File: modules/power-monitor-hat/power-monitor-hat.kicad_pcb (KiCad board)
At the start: 2 copper layers, 65 x 56 mm, 56 parts, among them J1 Barrel_Jack_Switch, J2 GPIO, J3 OutputTerminal, J4 OutputTerminal, J5 OutputTerminal, Q1 BC856BDW1, Q2 SI2301CDS, U1 NCP1117-3.3_SOT223, U2 CAT24C256, U3 INA219AxD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

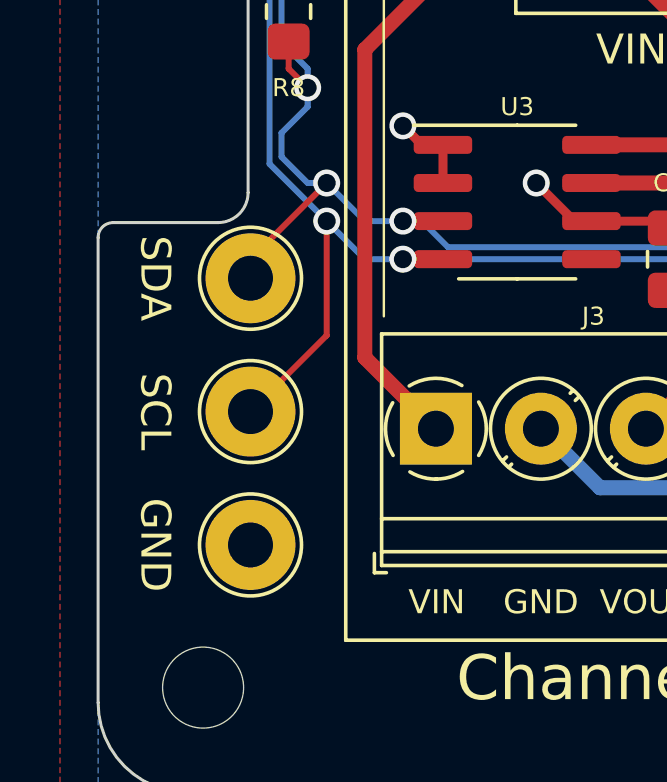
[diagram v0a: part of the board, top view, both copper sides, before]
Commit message: Use smaller footprint for test points
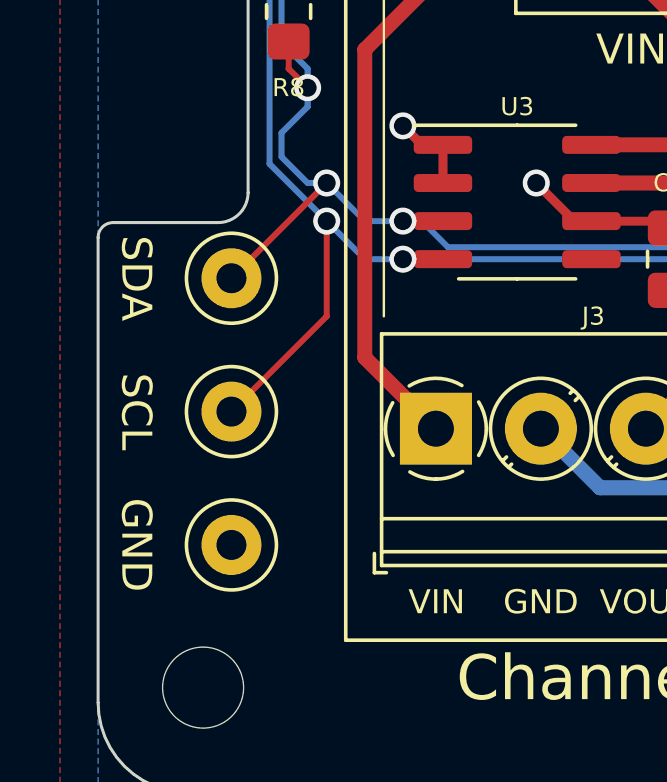
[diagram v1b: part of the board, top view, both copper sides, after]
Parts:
- TP1, TP2, TP3: footprint TestPoint:TestPoint_Loop_D2.54mm_Drill1.5mm_Beaded -> TestPoint:TestPoint_Loop_D1.80mm_Drill1.0mm_Beaded
- moved TP1 0.64 mm to (104.4, 91.7)
- moved TP2 0.64 mm to (104.4, 82.9)
- moved TP3 0.64 mm to (104.4, 87.3)
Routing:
- net /SDA: track 96.1 -> 97.0 mm
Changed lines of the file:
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@@
     )
   )
-  (footprint "TestPoint:TestPoint_Loop_D2.54mm_Drill1.5mm_Beaded" (layer "F.Cu")
-    (at 105.08 91.745)
-    (descr "wire loop with bead as test point, loop diameter2.548mm, hole diameter 1.5mm")
+  (footprint "TestPoint:TestPoint_Loop_D1.80mm_Drill1.0mm_Beaded" (layer "F.Cu")
+    (at 104.445 91.745)
+    (descr "wire loop with bead as test point, loop diameter 1.8mm, hole diameter 1.0mm")
     (tags "test point wire loop bead")
     (property "Sheetfile" "power-monitor-hat.kicad_sch")
@@
       (effects (font (size 0.6 0.6) (thickness 0.08)))
     )
-    (fp_circle (center 0 0) (end 1.7 0) (layer "F.SilkS") (width 0.12) (fill none))
-    (fp_circle (center 0 0) (end 2 0) (layer "F.CrtYd") (width 0.05) (fill none))
-    (fp_line (start -1.3 -0.3) (end -1.3 0.3) (layer "F.Fab") (width 0.12))
-    (fp_line (start 1.3 0.3) (end 1.3 -0.3) (layer "F.Fab") (width 0.12))
-    (fp_line (start -1.3 0.3) (end 1.3 0.3) (layer "F.Fab") (width 0.12))
-    (fp_line (start 1.3 -0.3) (end -1.3 -0.3) (layer "F.Fab") (width 0.12))
-    (fp_circle (center 0 0) (end 1.5 0) (layer "F.Fab") (width 0.12) (fill none))
-    (pad "1" thru_hole circle (at 0 0) (size 3 3) (drill 1.5) (layers *.Cu *.Mask)
+    (fp_circle (center 0 0) (end 1.5 0) (layer "F.SilkS") (width 0.12) (fill none))
+    (fp_circle (center 0 0) (end 1.8 0) (layer "F.CrtYd") (width 0.05) (fill none))
+    (fp_line (start 0.9 -0.2) (end 0.9 0.2) (layer "F.Fab") (width 0.12))
+    (fp_line (start 0.9 0.2) (end -0.9 0.2) (layer "F.Fab") (width 0.12))
+    (fp_line (start -0.9 -0.2) (end 0.9 -0.2) (layer "F.Fab") (width 0.12))
+    (fp_line (start -0.9 0.2) (end -0.9 -0.2) (layer "F.Fab") (width 0.12))
+    (fp_circle (center 0 0) (end 1.3 0) (layer "F.Fab") (width 0.12) (fill none))
+    (pad "1" thru_hole circle (at 0 0) (size 2 2) (drill 1) (layers *.Cu *.Mask)
       (net 1 "GND") (pinfunction "1") (pintype "passive"))
-    (model "${KICAD6_3DMODEL_DIR}/TestPoint.3dshapes/TestPoint_Loop_D2.54mm_Drill1.5mm_Beaded.wrl"
+    (model "${KICAD6_3DMODEL_DIR}/TestPoint.3dshapes/TestPoint_Loop_D1.80mm_Drill1.0mm_Beaded.wrl"
       (offset (xyz 0 0 0))
       (scale (xyz 1 1 1))
@@
     )
   )
-  (footprint "TestPoint:TestPoint_Loop_D2.54mm_Drill1.5mm_Beaded" (layer "F.Cu")
-    (at 105.08 87.3)
-    (descr "wire loop with bead as test point, loop diameter2.548mm, hole diameter 1.5mm")
+  (footprint "TestPoint:TestPoint_Loop_D1.80mm_Drill1.0mm_Beaded" (layer "F.Cu")
+    (at 104.445 87.3)
+    (descr "wire loop with bead as test point, loop diameter 1.8mm, hole diameter 1.0mm")
     (tags "test point wire loop bead")
     (property "Sheetfile" "power-monitor-hat.kicad_sch")
@@
       (effects (font (size 0.6 0.6) (thickness 0.08)))
     )
-    (fp_circle (center 0 0) (end 1.7 0) (layer "F.SilkS") (width 0.12) (fill none))
-    (fp_circle (center 0 0) (end 2 0) (layer "F.CrtYd") (width 0.05) (fill none))
-    (fp_line (start -1.3 -0.3) (end -1.3 0.3) (layer "F.Fab") (width 0.12))
-    (fp_line (start 1.3 -0.3) (end -1.3 -0.3) (layer "F.Fab") (width 0.12))
-    (fp_line (start -1.3 0.3) (end 1.3 0.3) (layer "F.Fab") (width 0.12))
-    (fp_line (start 1.3 0.3) (end 1.3 -0.3) (layer "F.Fab") (width 0.12))
-    (fp_circle (center 0 0) (end 1.5 0) (layer "F.Fab") (width 0.12) (fill none))
-    (pad "1" thru_hole circle (at 0 0) (size 3 3) (drill 1.5) (layers *.Cu *.Mask)
+    (fp_circle (center 0 0) (end 1.5 0) (layer "F.SilkS") (width 0.12) (fill none))
+    (fp_circle (center 0 0) (end 1.8 0) (layer "F.CrtYd") (width 0.05) (fill none))
+    (fp_line (start -0.9 -0.2) (end 0.9 -0.2) (layer "F.Fab") (width 0.12))
+    (fp_line (start -0.9 0.2) (end -0.9 -0.2) (layer "F.Fab") (width 0.12))
+    (fp_line (start 0.9 -0.2) (end 0.9 0.2) (layer "F.Fab") (width 0.12))
+    (fp_line (start 0.9 0.2) (end -0.9 0.2) (layer "F.Fab") (width 0.12))
+    (fp_circle (center 0 0) (end 1.3 0) (layer "F.Fab") (width 0.12) (fill none))
+    (pad "1" thru_hole circle (at 0 0) (size 2 2) (drill 1) (layers *.Cu *.Mask)
       (net 2 "/SCL") (pinfunction "1") (pintype "passive"))
-    (model "${KICAD6_3DMODEL_DIR}/TestPoint.3dshapes/TestPoint_Loop_D2.54mm_Drill1.5mm_Beaded.wrl"
+    (model "${KICAD6_3DMODEL_DIR}/TestPoint.3dshapes/TestPoint_Loop_D1.80mm_Drill1.0mm_Beaded.wrl"
       (offset (xyz 0 0 0))
       (scale (xyz 1 1 1))
@@
     )
   )
-  (footprint "TestPoint:TestPoint_Loop_D2.54mm_Drill1.5mm_Beaded" (layer "F.Cu")
-    (at 105.08 82.855)
-    (descr "wire loop with bead as test point, loop diameter2.548mm, hole diameter 1.5mm")
+  (footprint "TestPoint:TestPoint_Loop_D1.80mm_Drill1.0mm_Beaded" (layer "F.Cu")
+    (at 104.445 82.855)
+    (descr "wire loop with bead as test point, loop diameter 1.8mm, hole diameter 1.0mm")
     (tags "test point wire loop bead")
     (property "Sheetfile" "power-monitor-hat.kicad_sch")
@@
       (effects (font (size 0.6 0.6) (thickness 0.08)))
     )
-    (fp_circle (center 0 0) (end 1.7 0) (layer "F.SilkS") (width 0.12) (fill none))
-    (fp_circle (center 0 0) (end 2 0) (layer "F.CrtYd") (width 0.05) (fill none))
-    (fp_line (start 1.3 -0.3) (end -1.3 -0.3) (layer "F.Fab") (width 0.12))
-    (fp_line (start 1.3 0.3) (end 1.3 -0.3) (layer "F.Fab") (width 0.12))
-    (fp_line (start -1.3 -0.3) (end -1.3 0.3) (layer "F.Fab") (width 0.12))
-    (fp_line (start -1.3 0.3) (end 1.3 0.3) (layer "F.Fab") (width 0.12))
-    (fp_circle (center 0 0) (end 1.5 0) (layer "F.Fab") (width 0.12) (fill none))
-    (pad "1" thru_hole circle (at 0 0) (size 3 3) (drill 1.5) (layers *.Cu *.Mask)
+    (fp_circle (center 0 0) (end 1.5 0) (layer "F.SilkS") (width 0.12) (fill none))
+    (fp_circle (center 0 0) (end 1.8 0) (layer "F.CrtYd") (width 0.05) (fill none))
+    (fp_line (start -0.9 0.2) (end -0.9 -0.2) (layer "F.Fab") (width 0.12))
+    (fp_line (start 0.9 0.2) (end -0.9 0.2) (layer "F.Fab") (width 0.12))
+    (fp_line (start -0.9 -0.2) (end 0.9 -0.2) (layer "F.Fab") (width 0.12))
+    (fp_line (start 0.9 -0.2) (end 0.9 0.2) (layer "F.Fab") (width 0.12))
+    (fp_circle (center 0 0) (end 1.3 0) (layer "F.Fab") (width 0.12) (fill none))
+    (pad "1" thru_hole circle (at 0 0) (size 2 2) (drill 1) (layers *.Cu *.Mask)
       (net 43 "/SDA") (pinfunction "1") (pintype "passive"))
-    (model "${KICAD6_3DMODEL_DIR}/TestPoint.3dshapes/TestPoint_Loop_D2.54mm_Drill1.5mm_Beaded.wrl"
+    (model "${KICAD6_3DMODEL_DIR}/TestPoint.3dshapes/TestPoint_Loop_D1.80mm_Drill1.0mm_Beaded.wrl"
       (offset (xyz 0 0 0))
       (scale (xyz 1 1 1))
@@
   (via (at 129.21 77.775) (size 0.9) (drill 0.6) (layers "F.Cu" "B.Cu") (free) (net 1))
   (via (at 133.655 79.68) (size 0.9) (drill 0.6) (layers "F.Cu" "B.Cu") (free) (net 1))
-  (segment (start 107.62 80.95) (end 107.62 84.76) (width 0.2) (layer "F.Cu") (net 2))
   (segment (start 106.35 66.98) (end 105.715 66.345) (width 0.2) (layer "F.Cu") (net 2))
-  (segment (start 107.62 84.76) (end 105.08 87.3) (width 0.2) (layer "F.Cu") (net 2))
+  (segment (start 107.62 84.125) (end 104.445 87.3) (width 0.2) (layer "F.Cu") (net 2))
+  (segment (start 107.62 80.95) (end 107.62 84.125) (width 0.2) (layer "F.Cu") (net 2))
   (segment (start 130.545 82.22) (end 129.21 82.22) (width 0.2) (layer "F.Cu") (net 2))
   (segment (start 110.16 82.22) (end 111.495 82.22) (width 0.2) (layer "F.Cu") (net 2))
@@
   (segment (start 154.545 78.41) (end 159.69 78.41) (width 0.5) (layer "F.Cu") (net 38))
   (segment (start 158.42 65.71) (end 158.42 72.68) (width 0.5) (layer "F.Cu") (net 39))
-  (segment (start 107.62 79.68) (end 105.08 82.22) (width 0.2) (layer "F.Cu") (net 43))
   (segment (start 110.16 80.95) (end 111.495 80.95) (width 0.2) (layer "F.Cu") (net 43))
   (segment (start 106.35 74.965) (end 106.35 75.87) (width 0.2) (layer "F.Cu") (net 43))
@@
   (segment (start 149.595 79.68) (end 149.595 80.95) (width 0.2) (layer "F.Cu") (net 43))
   (segment (start 106.35 75.87) (end 106.985 76.505) (width 0.2) (layer "F.Cu") (net 43))
+  (segment (start 107.62 79.68) (end 104.445 82.855) (width 0.2) (layer "F.Cu") (net 43))
   (via (at 106.985 76.505) (size 0.9) (drill 0.6) (layers "F.Cu" "B.Cu") (net 43))
   (via (at 110.16 80.95) (size 0.9) (drill 0.6) (layers "F.Cu" "B.Cu") (net 43))

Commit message: Correct units
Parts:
- C2, C3: value 22u -> 10u
- R10, R12, R14, R3, R4: value 220R -> 470R
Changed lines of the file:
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@@
       (effects (font (size 0.6 0.6) (thickness 0.08)))
     )
-    (fp_text value "220R" (at 2.385 0) (layer "F.Fab")
+    (fp_text value "470R" (at 2.385 0) (layer "F.Fab")
       (effects (font (size 0.6 0.6) (thickness 0.08)))
     )
@@
       (effects (font (size 0.6 0.6) (thickness 0.08)))
     )
-    (fp_text value "22u" (at 0 -1.905) (layer "F.Fab")
+    (fp_text value "10u" (at 0 -1.905) (layer "F.Fab")
       (effects (font (size 0.6 0.6) (thickness 0.08)))
     )
@@
       (effects (font (size 0.6 0.6) (thickness 0.08)))
     )
-    (fp_text value "220R" (at 2.385 0) (layer "F.Fab")
+    (fp_text value "470R" (at 2.385 0) (layer "F.Fab")
       (effects (font (size 0.6 0.6) (thickness 0.08)))
     )
@@
       (effects (font (size 0.6 0.6) (thickness 0.08)))
     )
-    (fp_text value "220R" (at 3.175 0) (layer "F.Fab")
+    (fp_text value "470R" (at 3.175 0) (layer "F.Fab")
       (effects (font (size 0.6 0.6) (thickness 0.08)))
     )
@@
       (effects (font (size 0.6 0.6) (thickness 0.08)))
     )
-    (fp_text value "220R" (at 3.175 0) (layer "F.Fab")
+    (fp_text value "470R" (at 3.175 0) (layer "F.Fab")
       (effects (font (size 0.6 0.6) (thickness 0.08)))
     )
@@
       (effects (font (size 0.6 0.6) (thickness 0.08)))
     )
-    (fp_text value "220R" (at 3.175 0) (layer "F.Fab")
+    (fp_text value "470R" (at 3.175 0) (layer "F.Fab")
       (effects (font (size 0.6 0.6) (thickness 0.08)))
     )
@@
       (effects (font (size 0.6 0.6) (thickness 0.08)))
     )
-    (fp_text value "22u" (at 0 1.905) (layer "F.Fab")
-      (effects (font (size 0.6 0.6) (thickness 0.08)))
-    )
+    (fp_text value "10u" (at 0 1.905) (layer "F.Fab")
+      (effects (font (size 0.6 0.6) (thickness 0.08)))
+    )

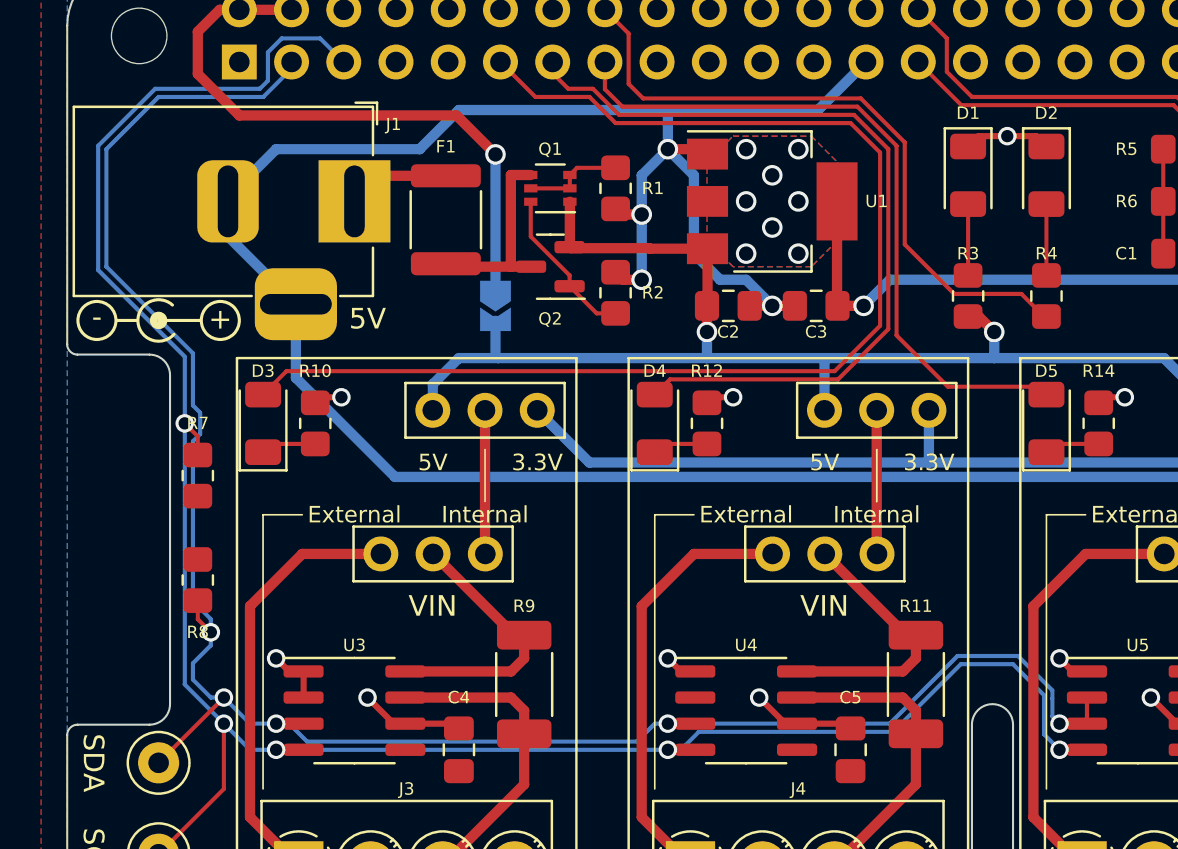
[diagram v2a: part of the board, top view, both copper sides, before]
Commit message: Prevent silk over via
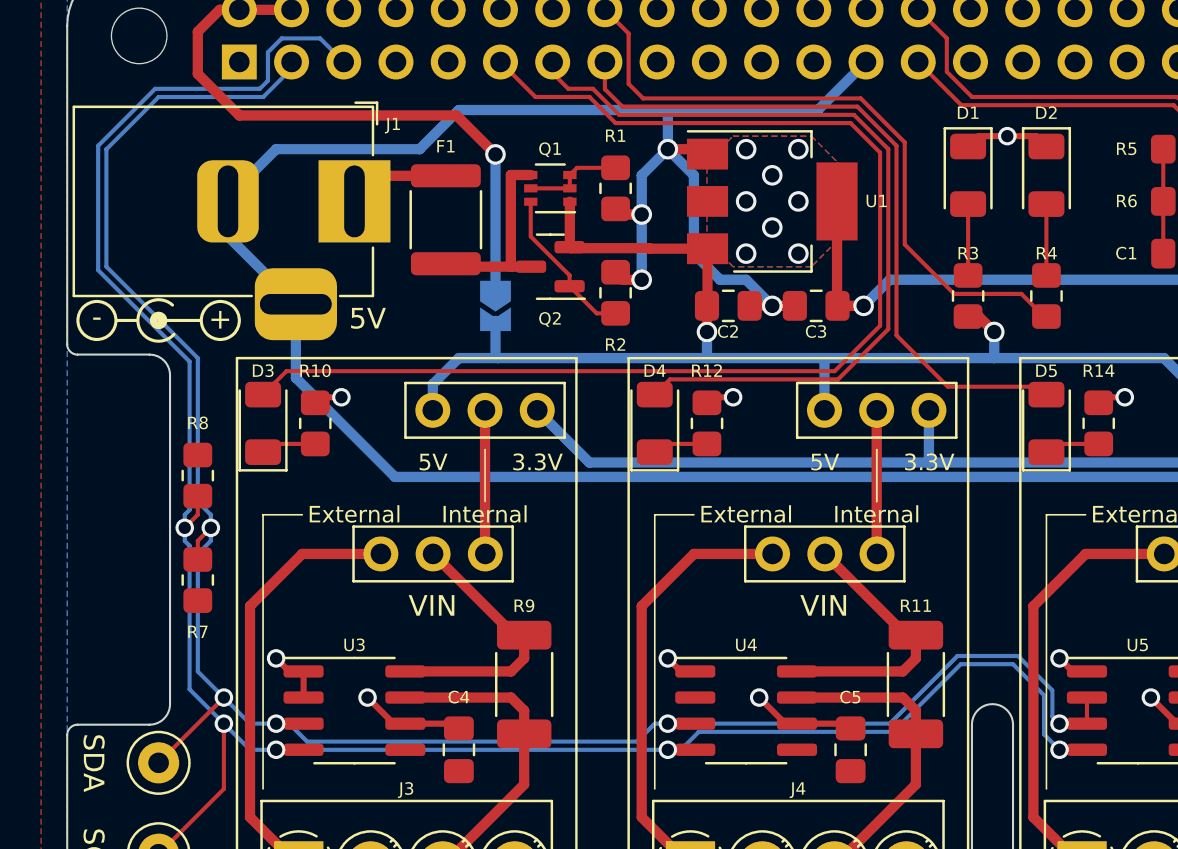
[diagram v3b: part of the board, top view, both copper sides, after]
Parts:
- turned R7 to 90 degrees
- turned R8 to -90 degrees
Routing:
- net /SDA: track 97.0 -> 96.1 mm

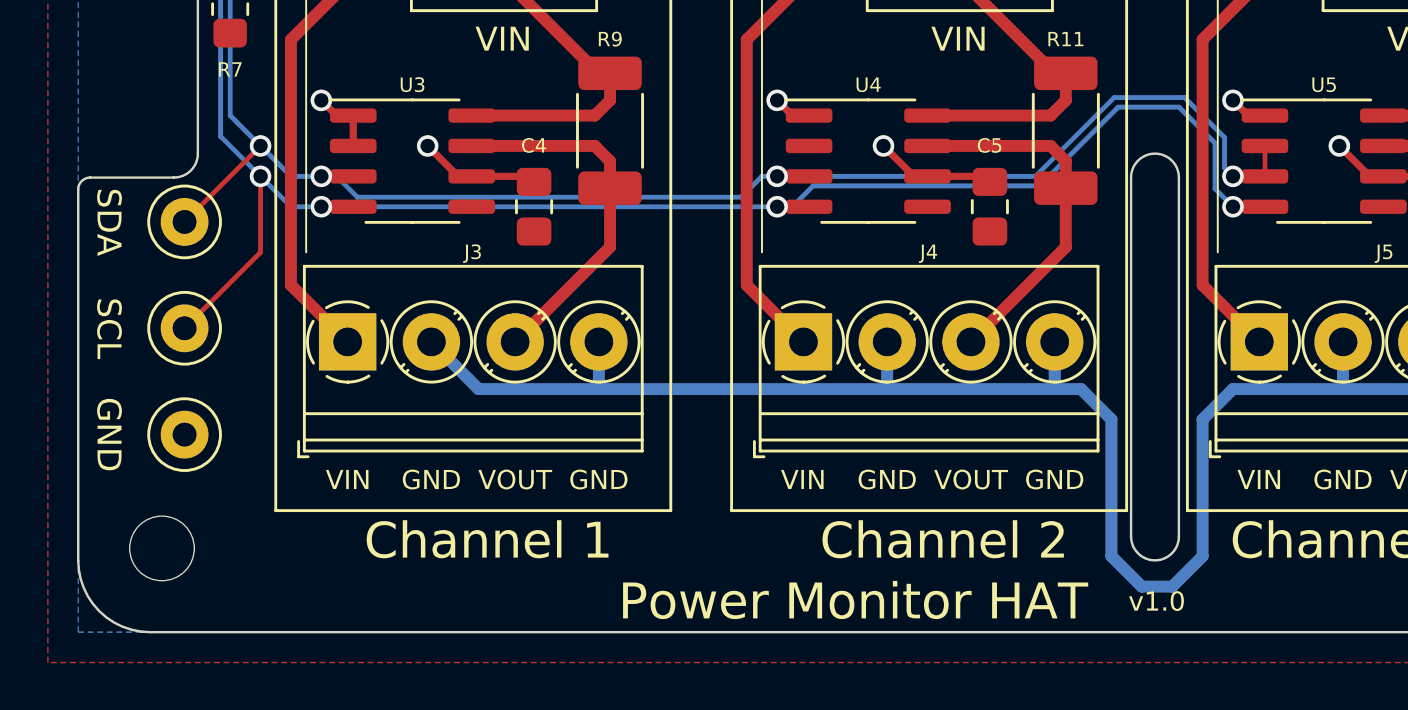
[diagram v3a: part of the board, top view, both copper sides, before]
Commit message: Silkscreen improvement
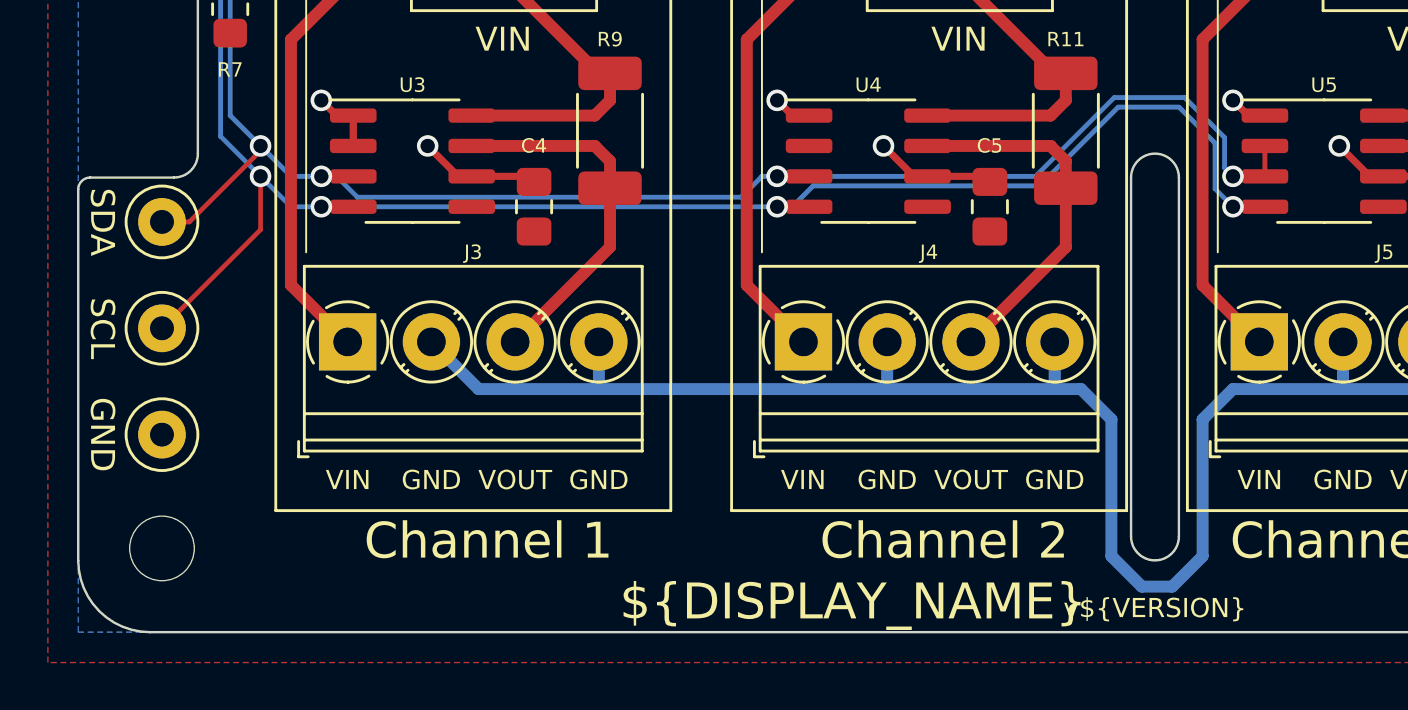
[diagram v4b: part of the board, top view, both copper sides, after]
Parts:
- SYM2: value OSHW-Logo2_7.3x6mm_SilkScreen -> OSHW-Logo2_9.8x8mm_SilkScreen; footprint Symbol:OSHW-Logo2_7.3x6mm_SilkScreen -> Symbol:OSHW-Logo2_9.8x8mm_SilkScreen
- SYM3: value KiCad-Logo2_5mm_SilkScreen -> KiCad-Logo2_6mm_SilkScreen; footprint Symbol:KiCad-Logo2_5mm_SilkScreen -> Symbol:KiCad-Logo2_6mm_SilkScreen
- moved SYM2 28.1 mm to (153.5, 95.5)
- moved SYM3 1.87 mm to (113.5, 94.5)
- moved TP1 0.94 mm to (103.5, 91.7)
- moved TP2 0.94 mm to (103.5, 82.9)
- moved TP3 0.94 mm to (103.5, 87.3)
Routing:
- net /SDA: track 96.1 -> 97.2 mm
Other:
- board text added: "${DISPLAY_NAME}"
- board text added: "${URL}"
- board text added: "RaspberryPI ${DISPLAY_NAME}"
- board text added: "v${VERSION}"
- board text removed: "Power Monitor HAT"
- board text removed: "v1.0"
